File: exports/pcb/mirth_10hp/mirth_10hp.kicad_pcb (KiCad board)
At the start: 2 copper layers, 50.8 x 128.5 mm, 1 part

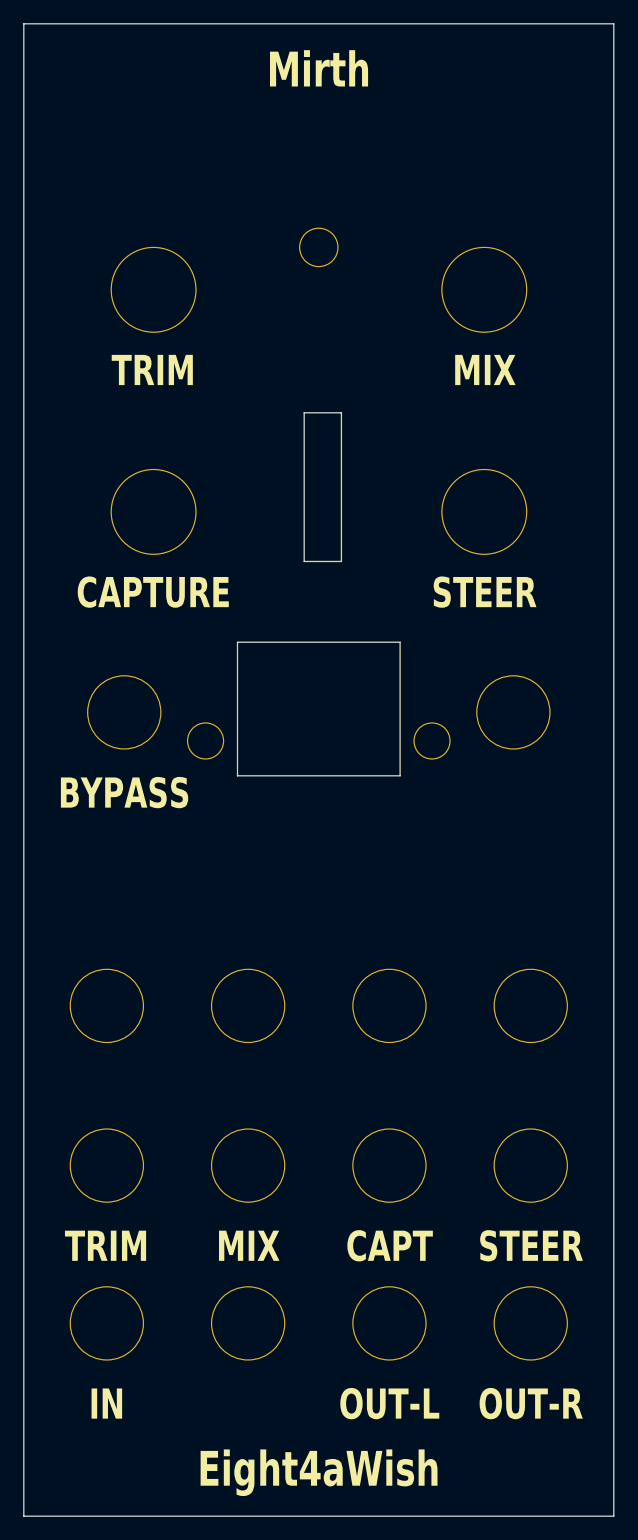
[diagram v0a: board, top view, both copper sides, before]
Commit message: Mirth: v1.1.0 labels — MIX, STEER/FREQ, RES, DRIVE, PATCH — and the six-row RUN page
The firmware's knobs moved on 2026-10-21 (1 MIX, 2 STEER or FREQ, 3 RES, 4 DRIVE; B7 steps
the patches). The CV_6 jack reads ST/FRQ: STEER/FREQ is 20 mm and the jacks sit 12 mm
apart. B7 is named a button by its hole, as Wish's is, since PATCH is not a button word.
New label STL, PCB faceplate and gerbers, and the render with v1.1.0's six-row screen.

Co-Authored-By: Claude Opus 5.5 <noreply@anthropic.com>
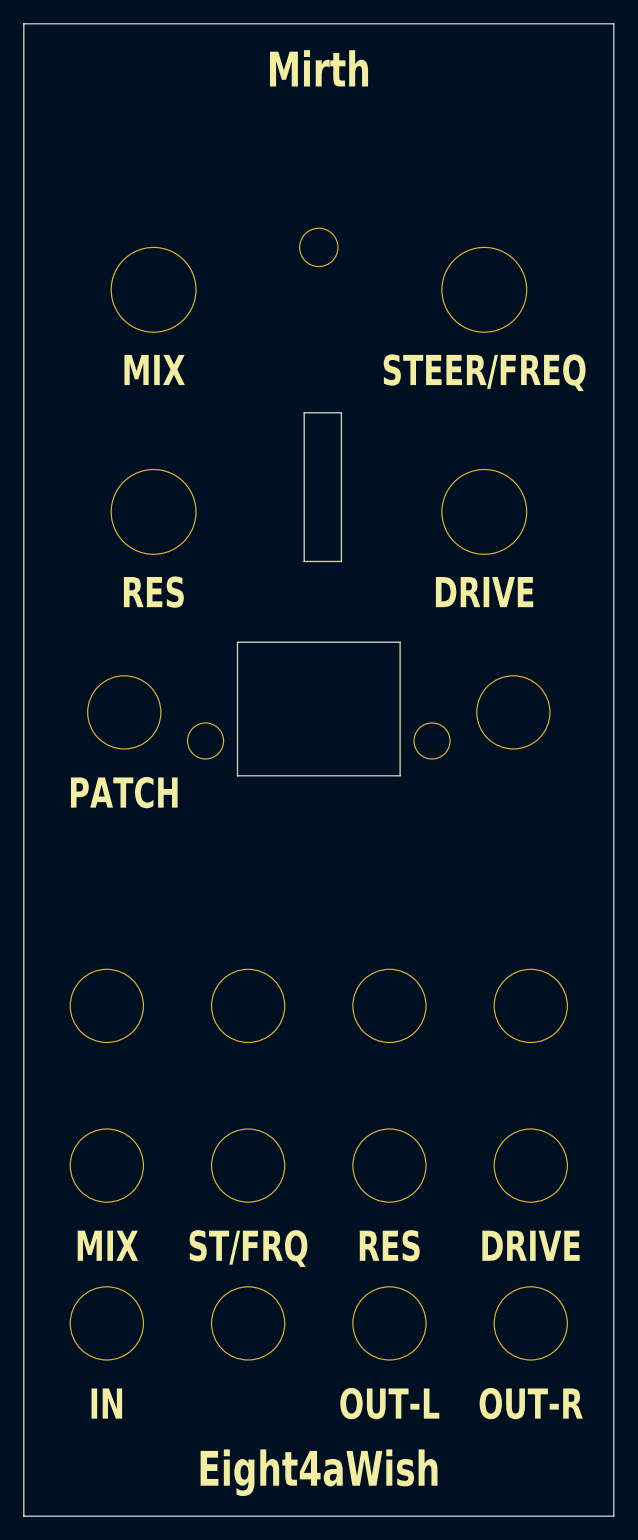
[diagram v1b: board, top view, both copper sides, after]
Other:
- board text added: "DRIVE"
- board text added: "PATCH"
- board text added: "RES"
- board text added: "ST/FRQ"
- board text added: "STEER/FREQ"
- board text removed: "BYPASS"
- board text removed: "CAPT"
- board text removed: "CAPTURE"
- board text removed: "STEER"
- board text removed: "TRIM"
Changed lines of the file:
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@@
 		(effects (font (size 2.6 1.872) (thickness 0.442) bold))
 	)
-	(gr_text "STEER" (at 43.65 105.311904) (layer "F.SilkS")
+	(gr_text "DRIVE" (at 43.65 105.311904) (layer "F.SilkS")
 		(effects (font (size 2.6 1.872) (thickness 0.442) bold))
 	)
-	(gr_text "CAPT" (at 31.483297 105.311904) (layer "F.SilkS")
+	(gr_text "RES" (at 31.483297 105.311904) (layer "F.SilkS")
 		(effects (font (size 2.6 1.872) (thickness 0.442) bold))
 	)
-	(gr_text "MIX" (at 19.316694 105.311904) (layer "F.SilkS")
+	(gr_text "ST/FRQ" (at 19.316694 105.311904) (layer "F.SilkS")
 		(effects (font (size 2.6 1.872) (thickness 0.442) bold))
 	)
-	(gr_text "TRIM" (at 7.149999 105.311904) (layer "F.SilkS")
+	(gr_text "MIX" (at 7.149999 105.311904) (layer "F.SilkS")
 		(effects (font (size 2.6 1.872) (thickness 0.442) bold))
 	)
-	(gr_text "BYPASS" (at 8.649995 66.288225) (layer "F.SilkS")
+	(gr_text "PATCH" (at 8.649995 66.288225) (layer "F.SilkS")
 		(effects (font (size 2.6 1.872) (thickness 0.442) bold))
 	)
-	(gr_text "STEER" (at 39.649996 49.027311) (layer "F.SilkS")
+	(gr_text "DRIVE" (at 39.649996 49.027311) (layer "F.SilkS")
 		(effects (font (size 2.6 1.872) (thickness 0.442) bold))
 	)
-	(gr_text "CAPTURE" (at 11.1755 49.027311) (layer "F.SilkS")
+	(gr_text "RES" (at 11.1755 49.027311) (layer "F.SilkS")
 		(effects (font (size 2.6 1.872) (thickness 0.442) bold))
 	)
-	(gr_text "MIX" (at 39.649996 29.904289) (layer "F.SilkS")
+	(gr_text "STEER/FREQ" (at 39.649996 29.904289) (layer "F.SilkS")
 		(effects (font (size 2.6 1.872) (thickness 0.442) bold))
 	)
-	(gr_text "TRIM" (at 11.1755 29.904289) (layer "F.SilkS")
+	(gr_text "MIX" (at 11.1755 29.904289) (layer "F.SilkS")
 		(effects (font (size 2.6 1.872) (thickness 0.442) bold))
 	)
